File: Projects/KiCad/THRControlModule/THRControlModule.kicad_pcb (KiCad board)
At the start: 2 copper layers, 9 parts, among them IC1 LTC1480CN8#PBF, IC2 LTC1480CN8#PBF, U1 MCP2515-I/P, U2 MCP2562-E-P, U4 MAX31856MUD+T

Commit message: 基板を更新
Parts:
- added C1: 0.1u, Capacitor_SMD:C_0603_1608Metric_Pad1.08x0.95mm_HandSolder, B.Cu at (125.2, 77.8)
- added C10: 0.01u, Capacitor_SMD:C_0603_1608Metric_Pad1.08x0.95mm_HandSolder, F.Cu at (73.8, 97.3)
- added C11: 0.1u, Capacitor_SMD:C_0603_1608Metric_Pad1.08x0.95mm_HandSolder, F.Cu at (73.6, 100.2)
- added C12: 0.01u, Capacitor_SMD:C_0603_1608Metric_Pad1.08x0.95mm_HandSolder, F.Cu at (73.3, 103.9)
- added C13: 0.1u, Capacitor_SMD:C_0603_1608Metric_Pad1.08x0.95mm_HandSolder, F.Cu at (60.3, 118.1)
- added C14: 0.1u, Capacitor_SMD:C_0603_1608Metric_Pad1.08x0.95mm_HandSolder, F.Cu at (55.9, 118.9)
- added C2: 0.1u, Capacitor_SMD:C_0603_1608Metric_Pad1.08x0.95mm_HandSolder, F.Cu at (133.5, 80.5)
- added C3: 0.1u, Capacitor_SMD:C_0603_1608Metric_Pad1.08x0.95mm_HandSolder, B.Cu at (117.9, 77.5)
- added C4: 0.1u, Capacitor_SMD:C_0603_1608Metric_Pad1.08x0.95mm_HandSolder, F.Cu at (125.4, 131.6)
- added C5: 0.1u, Capacitor_SMD:C_0603_1608Metric_Pad1.08x0.95mm_HandSolder, F.Cu at (111.4, 131.6)
- added C6: 0.1u, Capacitor_SMD:C_0603_1608Metric_Pad1.08x0.95mm_HandSolder, F.Cu at (151.8, 128.9)
- added C7: 0.1u, Capacitor_SMD:C_0603_1608Metric_Pad1.08x0.95mm_HandSolder, F.Cu at (149.9, 114.1)
- added C8: 15p, Capacitor_SMD:C_0603_1608Metric_Pad1.08x0.95mm_HandSolder, F.Cu at (163.1, 90.9)
- added C9: 15p, Capacitor_SMD:C_0603_1608Metric_Pad1.08x0.95mm_HandSolder, F.Cu at (156.3, 90.9)
- added D1: D, Diode_SMD:D_SOD-123, F.Cu at (55.4, 115.6)
- added D2: D, Diode_SMD:D_SOD-123, F.Cu at (30.4, 93.6)
- added D3: D, Diode_SMD:D_SOD-123, F.Cu at (55.4, 96.6)
- added H1: MountingHole, MountingHole:MountingHole_4.5mm, F.Cu at (151.3, 137.6)
- added H2: MountingHole, MountingHole:MountingHole_4.5mm, F.Cu at (151.3, 77.6)
- added H3: MountingHole, MountingHole:MountingHole_4.5mm, F.Cu at (91.3, 77.6)
- added H4: MountingHole, MountingHole:MountingHole_4.5mm, F.Cu at (91.3, 137.6)
- added J4: Conn_01x08, Hirose_Connector:Hirose_DF11B-8DP-2DS, F.Cu at (134.8, 134.6)
- added J6: Screw_Terminal_01x02, MAX31856MUD_T:RS_PRO_611-8157, F.Cu at (235.7, 96.0)
- added R1: 10k, Resistor_SMD:R_0603_1608Metric_Pad0.98x0.95mm_HandSolder, B.Cu at (125.2, 74.7)
- added R10: 10k, Resistor_SMD:R_0603_1608Metric_Pad0.98x0.95mm_HandSolder, F.Cu at (153.1, 114.1)
- added R11: 100, Resistor_SMD:R_0805_2012Metric_Pad1.20x1.40mm_HandSolder, F.Cu at (79.3, 88.2)
- added R12: 100, Resistor_SMD:R_0805_2012Metric_Pad1.20x1.40mm_HandSolder, F.Cu at (79.1, 92.2)
- added R13: 10k, Resistor_SMD:R_0603_1608Metric_Pad0.98x0.95mm_HandSolder, F.Cu at (60.4, 114.6)
- added R14: 10k, Resistor_SMD:R_0603_1608Metric_Pad0.98x0.95mm_HandSolder, F.Cu at (30.4, 98.6)
- added R15: 10k, Resistor_SMD:R_0603_1608Metric_Pad0.98x0.95mm_HandSolder, F.Cu at (55.4, 91.6)
- added R2: 10k, Resistor_SMD:R_0603_1608Metric_Pad0.98x0.95mm_HandSolder, F.Cu at (133.4, 77.5)
- added R3: 10k, Resistor_SMD:R_0603_1608Metric_Pad0.98x0.95mm_HandSolder, B.Cu at (117.9, 74.4)
- added R4: 1k, Resistor_SMD:R_0603_1608Metric_Pad0.98x0.95mm_HandSolder, B.Cu at (125.1, 71.6)
- added R5: 1k, Resistor_SMD:R_0603_1608Metric_Pad0.98x0.95mm_HandSolder, F.Cu at (133.4, 74.4)
- added R6: 1k, Resistor_SMD:R_0603_1608Metric_Pad0.98x0.95mm_HandSolder, B.Cu at (117.9, 71.0)
- added R7: 120, Resistor_SMD:R_0603_1608Metric_Pad0.98x0.95mm_HandSolder, F.Cu at (118.0, 131.6)
- added R8: 120, Resistor_SMD:R_0603_1608Metric_Pad0.98x0.95mm_HandSolder, F.Cu at (104.0, 131.6)
- added R9: 120, Resistor_SMD:R_0603_1608Metric_Pad0.98x0.95mm_HandSolder, F.Cu at (159.4, 130.8)
- added Y1: 8MHz, Crystal:Crystal_HC49-U_Vertical, F.Cu at (162.1, 86.0)
- moved U3 181.4 mm to (88.5, 88.9)
- moved IC2 154.8 mm to (107.7, 124.9), turned to -90 degrees
- moved LS1 153.9 mm to (96.4, 108.7)
- moved IC1 132.7 mm to (121.7, 124.9), turned to -90 degrees
- moved A1 99.2 mm to (129.2, 97.0), turned to 180 degrees
- moved U1 88.4 mm to (163.2, 121.2), turned to -90 degrees
- moved U2 76.9 mm to (155.7, 94.9), turned to 180 degrees
- renumbered U2 to U1, U1 to U2, U4 to U3
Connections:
- U1 pad 2: unconnected-(U2-VSS-Pad2) -> GND
- U2 pad 18: +3V3 -> +3.3V
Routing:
- net +3.3V: track 0.00 -> 82.9 mm, vias 0 -> 1
- net +5V: track 0.00 -> 67.7 mm
- net CAN__L: track 0.00 -> 23.3 mm
- net CAN__H: track 0.00 -> 23.2 mm
- net OCS2: track 0.00 -> 16.6 mm
- net OCS1: track 0.00 -> 12.0 mm
- net CAN__RXD-CANRX: track 0.00 -> 11.7 mm
- net Net-(C3-Pad1): track 0.00 -> 7.99 mm
- net Net-(C1-Pad1): track 0.00 -> 7.73 mm
- net Net-(C2-Pad1): track 0.00 -> 7.63 mm
- net CAN__TXD-TXCAN: track 0.00 -> 5.99 mm
- net B3M_Servo__Open: track 0.00 -> 5.67 mm
- net RS485__B1: track 0.00 -> 5.21 mm
- net RS485__B2: track 0.00 -> 5.19 mm
- net RS485__A1: track 0.00 -> 4.49 mm
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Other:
- board outline added: 110 x 95 mm

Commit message: DF1Bシリーズとしてまとめた。
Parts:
- added D4: D, Diode_SMD:D_SOD-123, B.Cu at (138.3, 127.8)
- added D5: LED, LED_SMD:LED_0603_1608Metric_Pad1.05x0.95mm_HandSolder, F.Cu at (142.4, 130.0)
- added J1: Conn_01x04, Hirose_Connector:Hirose_DF1BZ-4P-2.5DS, F.Cu at (121.4, 137.6)
- added J2: Conn_01x04, Hirose_Connector:Hirose_DF1BZ-4P-2.5DS, F.Cu at (107.3, 137.6)
- added J3: Conn_01x04, Hirose_Connector:Hirose_DF1BZ-4P-2.5DS, F.Cu at (80.0, 124.3)
- added J5: Conn_01x06, Hirose_Connector:DF1BZ-6P-2.5DS, F.Cu at (140.1, 68.1)
- added R16: 1k, Resistor_SMD:R_0603_1608Metric_Pad0.98x0.95mm_HandSolder, F.Cu at (133.3, 130.2)
- C7, JP1, JP2, R10: moved to B.Cu
- Y1: footprint Crystal:Crystal_HC49-U_Vertical -> Crystal:Crystal_HC49-4H_Vertical
- moved JP1 164.4 mm to (98.1, 76.4), turned to 90 degrees
- moved J6 158.5 mm to (77.3, 100.0), turned to 90 degrees
- moved JP2 158.2 mm to (102.0, 68.9), turned to 90 degrees
- moved D2 78.8 mm to (108.4, 82.4), turned to 180 degrees
- moved R14 74.9 mm to (103.3, 81.6)
- moved D1 64.9 mm to (108.4, 78.2), turned to 180 degrees
- moved D3 57.7 mm to (108.4, 73.9), turned to 180 degrees
- moved R13 56.3 mm to (103.3, 78.1)
- moved R15 50.8 mm to (103.3, 74.6)
- moved C14 48.8 mm to (97.1, 92.8), turned to 180 degrees
- moved C13 48.4 mm to (101.6, 92.8), turned to 180 degrees
- moved LS1 44.8 mm to (140.7, 115.1), turned to 90 degrees
- moved C12 21.2 mm to (88.7, 89.4), turned to 90 degrees
- moved C10 18.9 mm to (88.7, 85.7), turned to 90 degrees
- moved C11 14.7 mm to (83.7, 89.5), turned to -90 degrees
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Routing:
- net SPI__MISO: track 0.00 -> 133.8 mm
- net SPI__SCLK: track 0.00 -> 109.3 mm, vias 0 -> 1
- net +12V: track 0.00 -> 98.2 mm, vias 0 -> 1
- net SPI__MOSI: track 0.00 -> 93.0 mm
- net Umbilical__LaunchPinInput: track 0.00 -> 91.4 mm
- net +3.3V: track 82.9 -> 173.4 mm, vias 1 -> 4
- net Umbilical__WaitingPinInput: track 0.00 -> 81.4 mm, vias 0 -> 1
- net MAX31856__~{CS}-~{CS}: track 0.00 -> 53.1 mm
- net RS485__RO-RX: track 0.00 -> 51.0 mm, vias 0 -> 2
- net MCP2515__~{CS}-~{CS}: track 0.00 -> 45.7 mm, vias 0 -> 1
- net RS485__Enable_RS405: track 3.01 -> 48.1 mm, vias 0 -> 1
- net RS485__DI-TX: track 0.00 -> 43.8 mm, vias 0 -> 1
- net RS485__Enable_B3M: track 3.09 -> 44.1 mm, vias 0 -> 1
- net +5V: track 67.7 -> 106.9 mm, vias 0 -> 2
- net MAX31856__DRDY-DRDY: track 0.00 -> 39.0 mm
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
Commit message: Kicadの更新
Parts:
- removed J5: Conn_01x06, Hirose_Connector:DF1BZ-6P-2.5DS
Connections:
- A1 pad 30: +12V -> 12Vin
- D4 pad 1: +12V -> 12Vin
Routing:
- net IO__Busser: track 0.00 -> 40.6 mm, vias 0 -> 3
- net 12Vin: track 0.00 -> 39.3 mm
- net +5V: track 106.9 -> 67.7 mm, vias 2 -> 0
- net +12V: track 98.2 -> 60.4 mm
- net MAX31855__~{CS}-~{CS}: track 19.2 -> 0.00 mm
- net Net-(U3-T+): track 7.71 -> 21.4 mm
- net SPI__MISO: track 133.8 -> 121.3 mm, vias 0 -> 1
- net SPI__SCLK: track 109.3 -> 99.3 mm, vias 1 -> 0
- net GND: track 0.00 -> 9.22 mm, vias 0 -> 68
- net MAX31856__FAULT-FAULT: track 34.9 -> 37.2 mm, vias 0 -> 4
- net MAX31856__~{CS}-~{CS}: track 53.1 -> 55.2 mm, vias 0 -> 4
- net Net-(JP2-A): track 21.5 -> 22.8 mm
- net MAX31856__DRDY-DRDY: track 39.0 -> 40.1 mm, vias 0 -> 2
- net Net-(D2-A): track 14.2 -> 13.6 mm
- added copper zone on B.Cu, net GND
- added copper zone on F.Cu, net GND
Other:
- board text added: "B3M-SC-1170"
- board text added: "CAN-BUS"
- board text added: "RS405CB"

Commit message: 基板を更新（最終確認中）
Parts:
- added C10: 0.1u, Capacitor_SMD:C_0603_1608Metric_Pad1.08x0.95mm_HandSolder, B.Cu at (102.3, 103.8)
- added D1: LED, LED_SMD:LED_0603_1608Metric_Pad1.05x0.95mm_HandSolder, F.Cu at (96.0, 102.7)
- added D2: LED, LED_SMD:LED_0603_1608Metric_Pad1.05x0.95mm_HandSolder, F.Cu at (95.9, 99.6)
- added D3: LED, LED_SMD:LED_0603_1608Metric_Pad1.05x0.95mm_HandSolder, F.Cu at (96.0, 105.9)
- added G***: LOGO, LOGO, B.Cu at (134.6, 78.6)
- added J5: Conn_01x04, Hirose_Connector:Hirose_DF1BZ-4P-2.5DS, F.Cu at (82.9, 129.8)
- added R1: 1k, Resistor_SMD:R_0603_1608Metric_Pad0.98x0.95mm_HandSolder, F.Cu at (107.8, 92.3)
- added R15: 10k, Resistor_SMD:R_0603_1608Metric_Pad0.98x0.95mm_HandSolder, B.Cu at (102.3, 100.7)
- added R16: 1k, Resistor_SMD:R_0603_1608Metric_Pad0.98x0.95mm_HandSolder, B.Cu at (102.3, 97.6)
- added R2: 1k, Resistor_SMD:R_0603_1608Metric_Pad0.98x0.95mm_HandSolder, F.Cu at (107.8, 89.3)
- added R4: 1k, Resistor_SMD:R_0603_1608Metric_Pad0.98x0.95mm_HandSolder, F.Cu at (107.8, 95.2)
- R9: renamed from R16; moved to B.Cu
- moved J3 7.50 mm to (77.8, 117.1), turned to -75 degrees
- turned R9 to 90 degrees
- renumbered C4 to C1, C13 to C11, C14 to C12, C10 to C13, C11 to C14, C12 to C15, C5 to C2, C7 to C3, C1 to C4, C8 to C5, C9 to C6, C2 to C7, C6 to C8, C3 to C9, D1 to D6, D2 to D7, D3 to D8, R2 to R10, R5 to R11, R3 to R12, R6 to R13, R9 to R14, R15 to R17, R11 to R18, R14 to R19, R13 to R20, R12 to R21, R7 to R3, R8 to R5, R1 to R6, R4 to R7, R10 to R8, U2 to U1, U1 to U2
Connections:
- A1 pad 21: RS405_Servo__Open -> O__OrangeLED
- A1 pad 22: RS405_Servo__Close -> O__RedLED
- A1 pad 26: unconnected-(A1-A7-Pad26) -> O__BlueLED
- A1 pad 8: MAX31855__~{CS}-~{CS} -> unconnected-(A1-D5-Pad8)
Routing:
- net B3M_Servo__OpenInput: track 0.00 -> 71.5 mm
- net B3M_Servo__CloseInput: track 0.00 -> 51.1 mm
- net B3M_Servo__Close: track 0.00 -> 31.3 mm
- net O__OrangeLED: track 0.00 -> 20.8 mm
- net Net-(D3-A): track 0.00 -> 18.3 mm
- net Net-(D1-A): track 0.00 -> 16.6 mm
- net Net-(D2-A): track 0.00 -> 15.4 mm
- net O__RedLED: track 0.00 -> 14.8 mm, vias 0 -> 1
- net O__BlueLED: track 0.00 -> 11.3 mm
- net Net-(C10-Pad1): track 0.00 -> 6.98 mm
- net +3.3V: track 173.3 -> 176.2 mm
- net +12V: track 60.4 -> 58.6 mm, vias 1 -> 0
- net Net-(D8-A): track 23.7 -> 22.7 mm
- net IO__Busser: track 40.6 -> 41.5 mm
- net Net-(D5-A): track 9.93 -> 10.8 mm, vias 0 -> 1
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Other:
- board text added: "LaunchMode"
- board text added: "LimitSwitch"
- board text added: "Umbilical"
- board text added: "WaitingMode"

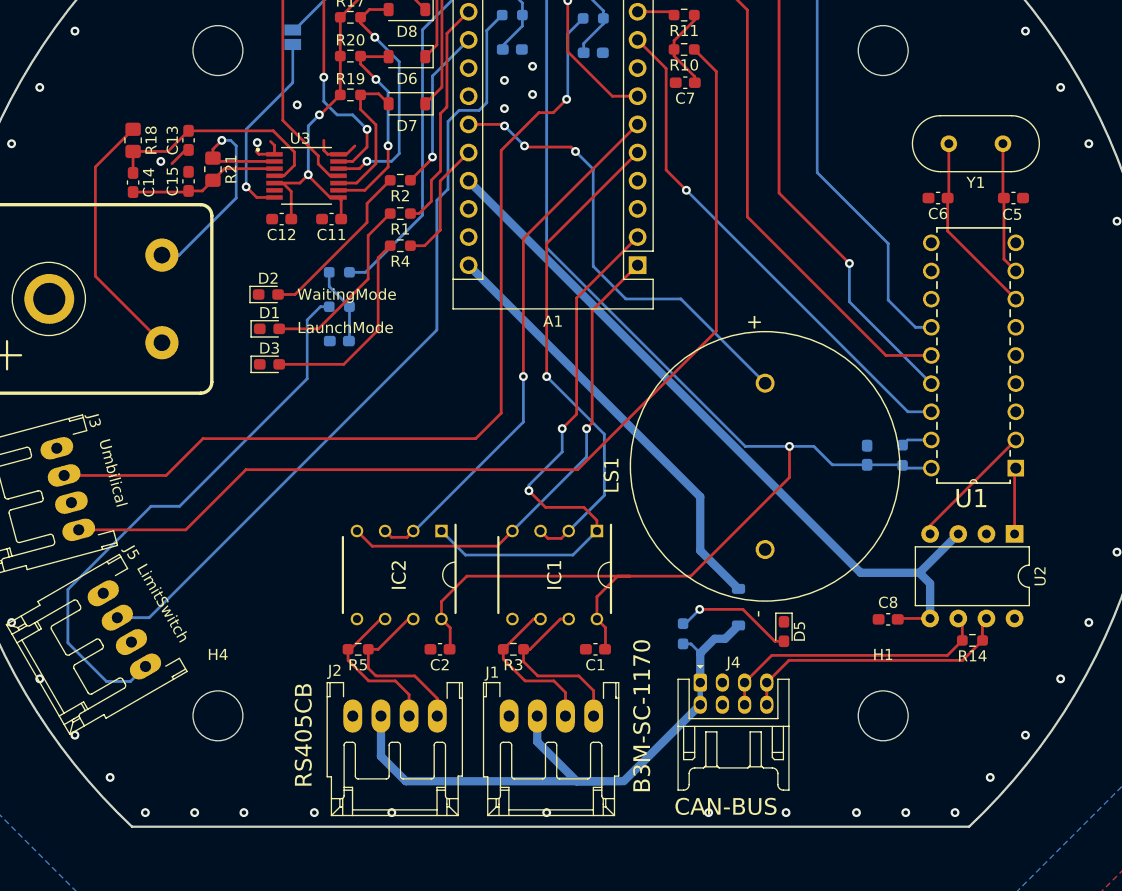
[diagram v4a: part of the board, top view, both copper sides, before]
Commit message: ValveControlModuleのガーバーデータを追加
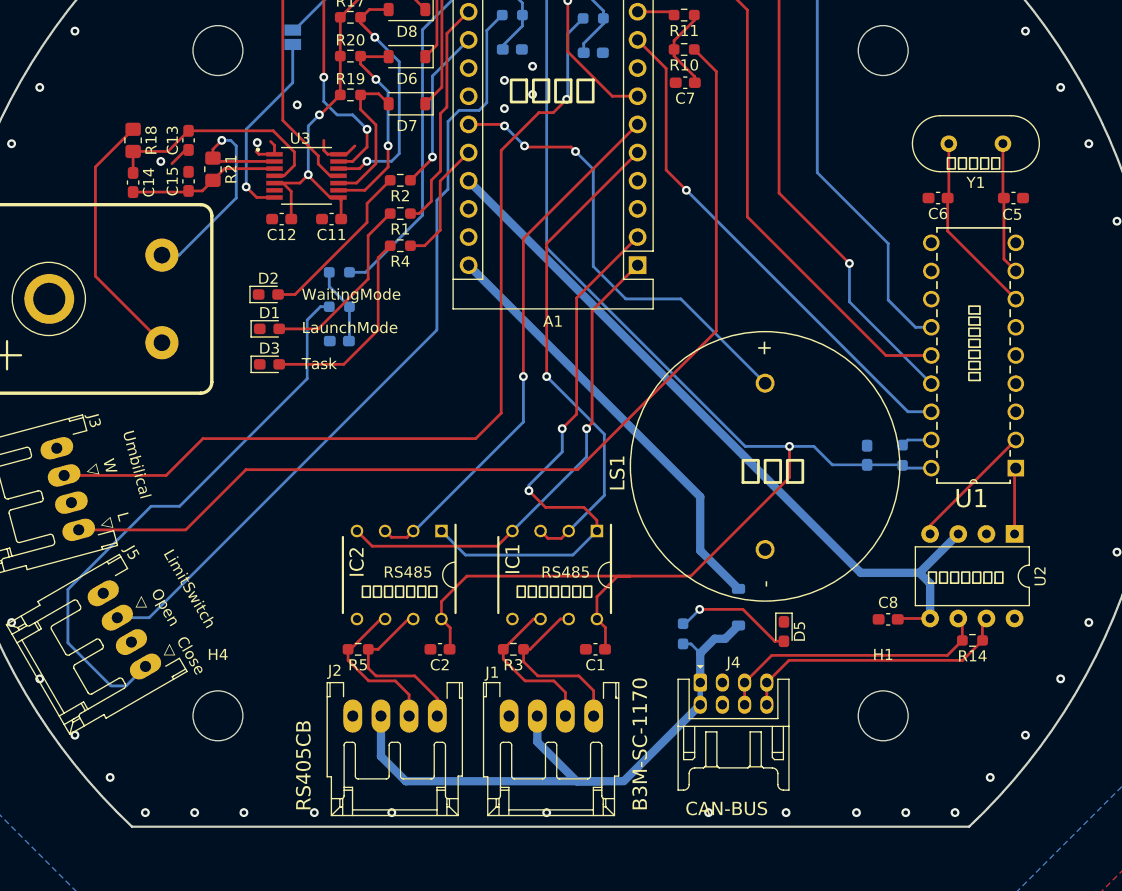
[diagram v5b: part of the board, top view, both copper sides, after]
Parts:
- added G***: LOGO, LOGO, B.Cu at (138.7, 66.9)
- moved G*** 13.4 mm to (133.7, 92.0)
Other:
- board text added: "Close"
- board text added: "Desinged by H.Tsutsumi"
- board text added: "H-58 Avionics"
- board text added: "L"
- board text added: "Open"
- board text added: "RS485"
- board text added: "Task"
- board text added: "ValveControl Module Build 2"
- board text added: "W"
- board text added: "△"
- board text added: "きゃんつうしん"
- board text added: "くりすたる"
- board text added: "とらんしーばー"
- board text added: "ぶざー"
- board text added: "まいこん"
